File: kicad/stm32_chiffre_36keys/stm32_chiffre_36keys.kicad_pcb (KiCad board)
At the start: 2 copper layers, 227.4 x 84.9 mm, 118 parts, among them J1 USB_C_Receptacle_USB2.0, J101 Conn_01x03_Female, J2 OLED I2C, SW1 SW_Push, SW10 SW_Push, SW11 SW_Push, SW12 SW_Push, SW13 SW_Push, SW14 SW_Push, SW15 SW_Push, SW16 SW_Push, SW17 SW_Push, SW18 SW_Push, SW19 SW_Push, SW2 SW_Push, SW20 SW_Push, SW21 SW_Push, SW22 SW_Push, SW23 SW_Push, SW24 SW_Push, SW25 SW_Push, SW26 SW_Push, SW27 SW_Push, SW28 SW_Push, SW29 SW_Push, SW3 SW_Push, SW30 SW_Push, SW31 SW_Push, SW32 SW_Push, SW33 SW_Push, SW34 SW_Push, SW35 SW_Push, SW36 Rotary_Encoder_Switch, SW37 SKQGABE010, SW38 SW_Push, SW39 SW_Push, SW4 SW_Push, SW40 SW_Push, SW41 SW_Push, SW42 SW_Push, SW43 SW_Push, SW5 SW_Push, SW6 SW_Push, SW7 SW_Push, SW8 SW_Push, SW9 SW_Push, U1 STM32F072CBT6, U2 PRTR5V0U2X, U3 XC6206PxxxMR-Regulator_Linear

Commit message: minor touch ups
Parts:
- moved D37 2.18 mm to (194.2, 123.5), turned to 97 degrees
- moved D32 0.83 mm to (100.2, 123.5)
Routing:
- net row3: track 204.8 -> 202.2 mm
- net +5V: track 596.6 -> 594.2 mm
- net Net-(D37-K): track 15.3 -> 14.8 mm
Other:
- board text added: "Le Chiffre stm32 v0.3 by sporkus"
- board text removed: "Le Chiffre 32 v0.3 by sporkus"

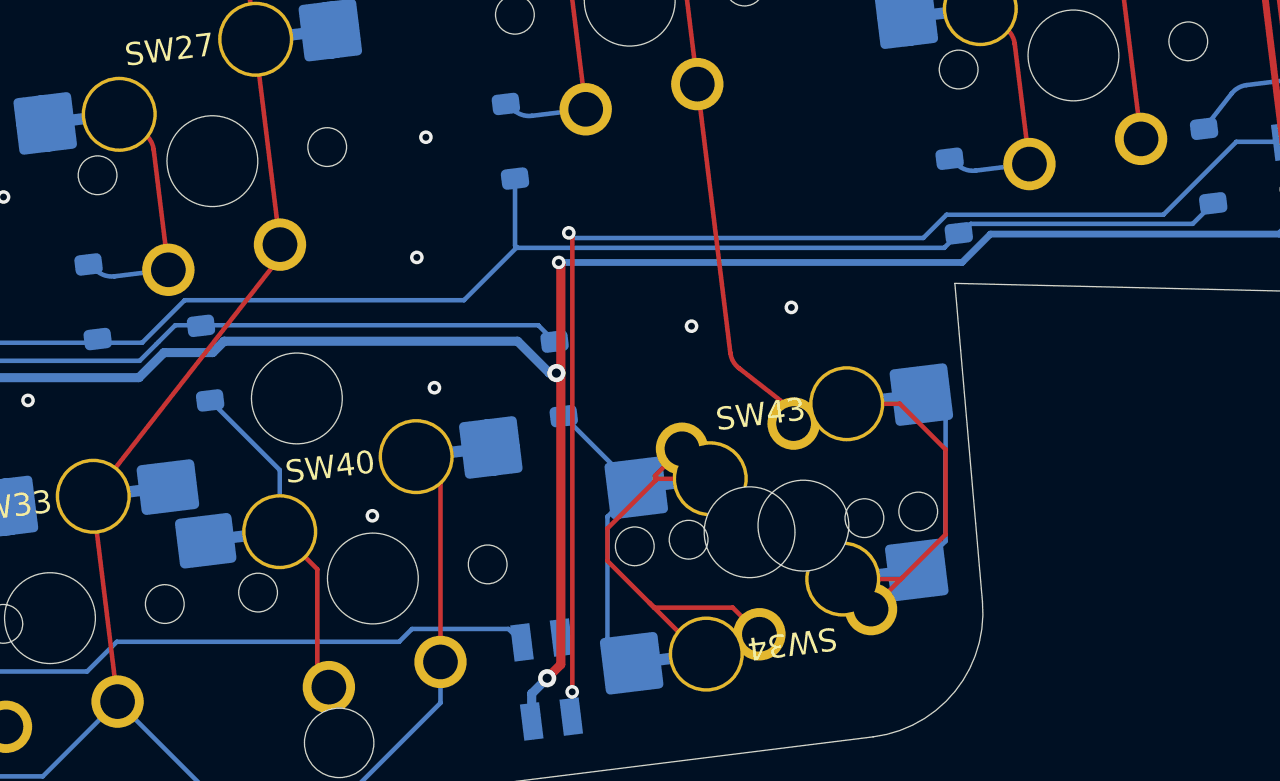
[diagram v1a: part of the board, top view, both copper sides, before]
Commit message: fix schematic on right thumb keys
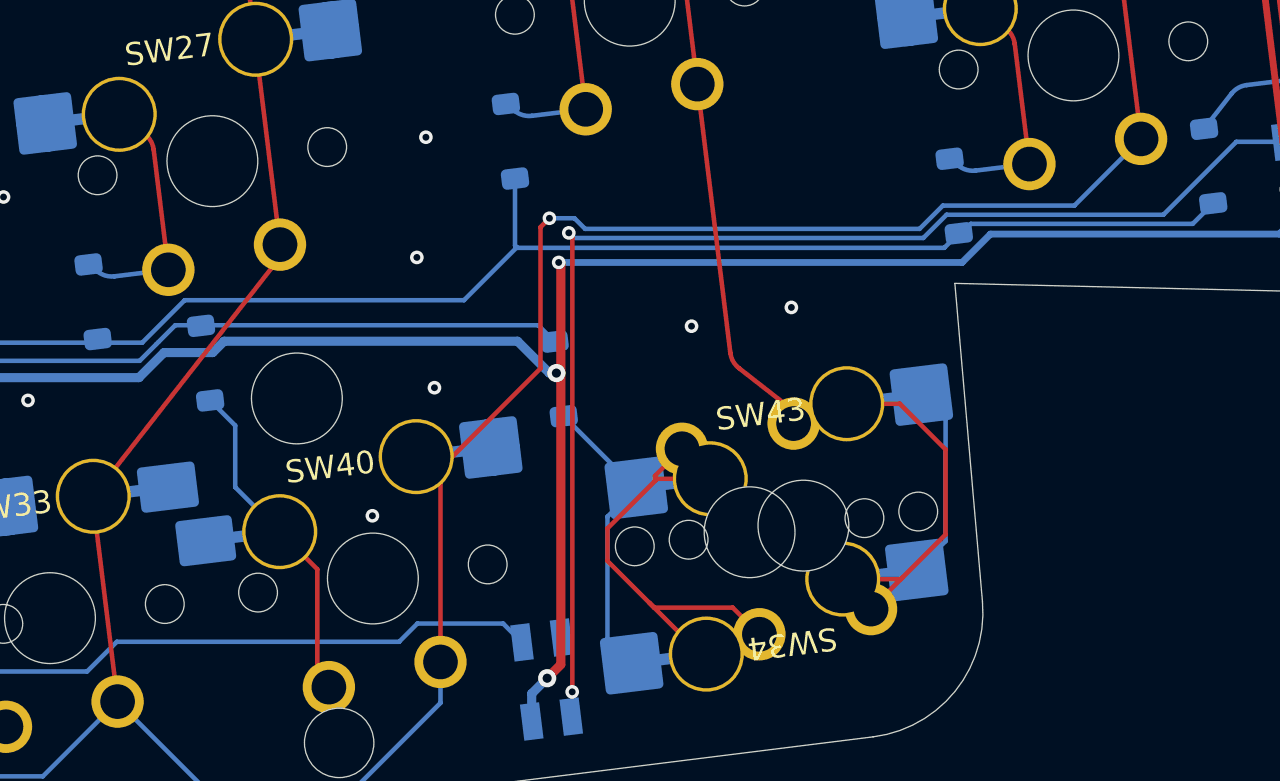
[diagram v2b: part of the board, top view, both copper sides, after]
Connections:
- D29 pad 1: Net-(D29-K) -> col7
- SW29 pad 1: Net-(D29-K) -> col7
- SW40 pad 2: col6 -> col8
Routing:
- net col8: track 140.9 -> 192.0 mm, vias 1 -> 2
- net col7: track 176.1 -> 185.9 mm
- net Net-(D29-K): track 9.77 -> 0.00 mm
- net col6: track 187.8 -> 178.3 mm
